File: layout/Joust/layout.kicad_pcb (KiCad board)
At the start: 4 copper layers, 30 x 30 mm, 56 parts, among them J1 B2B-PH-SM4-TB, J2 B2B-PH-SM4-TB, J3 TC2030-IDC-NL, J4 USB4105-GF-A, Q1 2N7002KT1G, Q2 2N7002KT1G, Q3 2N7002KT1G, U1 LSM6DSOXTR, U2 NORA-B206-00B, U3 BQ25185DLHR, U4 RT9013-33GB, U5 TPD4E05U06QDQARQ1, Y1 32.768kHz 7pF

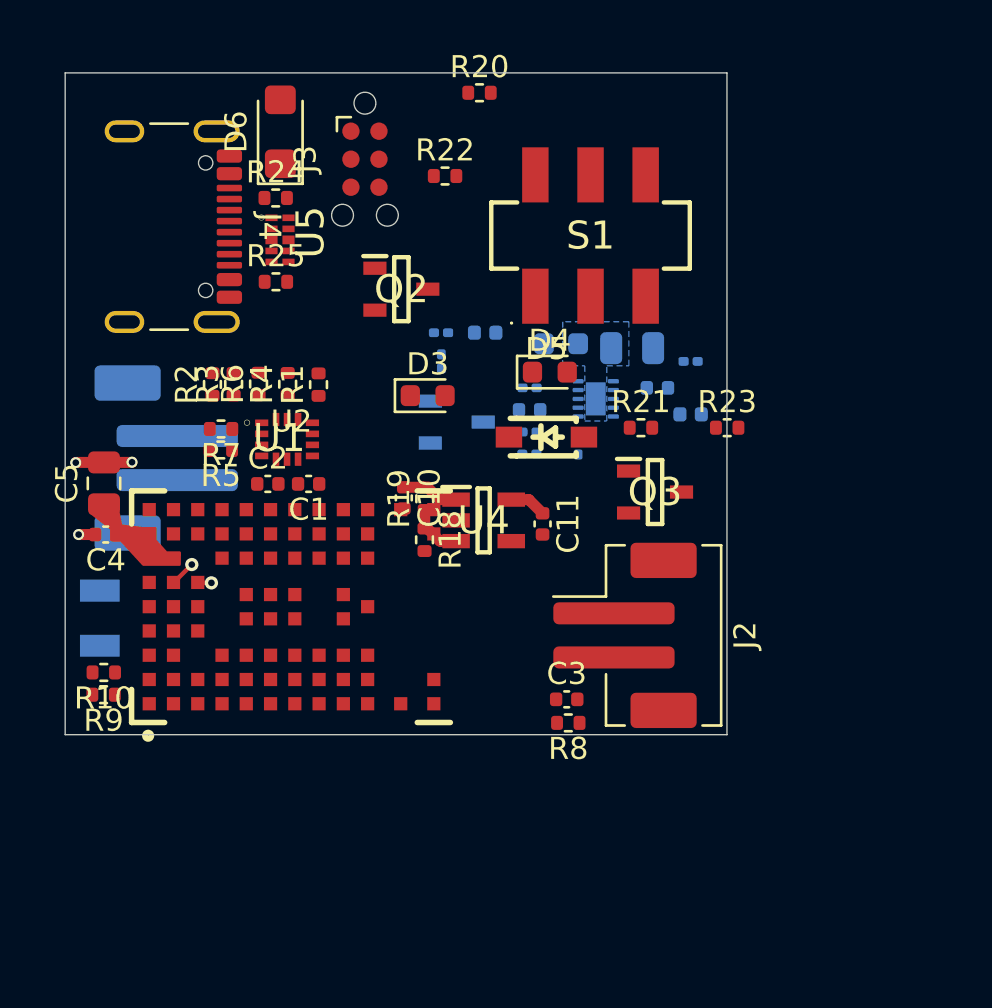
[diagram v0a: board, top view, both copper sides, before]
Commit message: remove bad traces
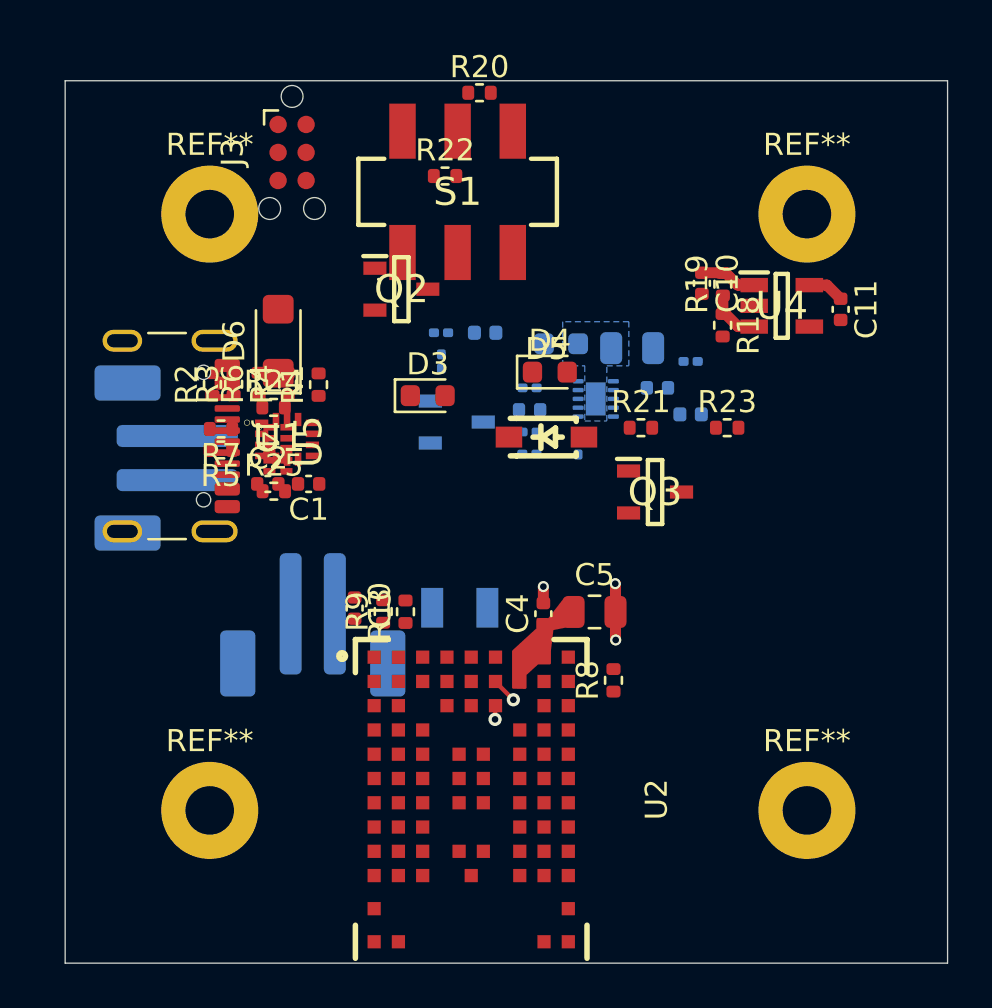
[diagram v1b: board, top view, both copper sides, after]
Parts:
- added REF**: MountingHole_2.2mm_M2_Pad, MountingHole:MountingHole_2.2mm_M2_Pad, F.Cu at (55.2, 65.9)
- added REF**: MountingHole_2.2mm_M2_Pad, MountingHole:MountingHole_2.2mm_M2_Pad, F.Cu at (82.2, 65.9)
- added REF**: MountingHole_2.2mm_M2_Pad, MountingHole:MountingHole_2.2mm_M2_Pad, F.Cu at (82.2, 93.0)
- added REF**: MountingHole_2.2mm_M2_Pad, MountingHole:MountingHole_2.2mm_M2_Pad, F.Cu at (55.2, 93.0)
- J2: moved to B.Cu
- moved C5 23.0 mm to (72.6, 84.0), turned to 0 degrees
- moved C4 20.2 mm to (70.3, 84.1), turned to 90 degrees
- moved C10 16.6 mm to (77.5, 69.1)
- moved C11 16.6 mm to (83.8, 70.3)
- moved R18 16.6 mm to (78.4, 71.0)
- moved R19 16.6 mm to (78.4, 69.1)
- moved U4 16.6 mm to (81.1, 70.1)
- moved Y1 16.3 mm to (66.5, 83.8), turned to 0 degrees
- moved J2 14.2 mm to (59.8, 84.6), turned to 0 degrees
- moved R10 13.9 mm to (64.0, 84.0), turned to 90 degrees
- moved R9 13.2 mm to (63.0, 84.0), turned to 90 degrees
- moved U2 11.9 mm to (67.0, 92.5), turned to -90 degrees
- moved C3 10.5 mm to (61.7, 83.8), turned to -90 degrees
- moved D6 9.49 mm to (58.3, 71.7)
- moved J4 9.49 mm to (52.3, 76.0)
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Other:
- board size 30 x 30 mm -> 40 x 40 mm
- copper layers 4 -> 2

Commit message: layout: 4-layer stackup, schematic placement, initial board sync
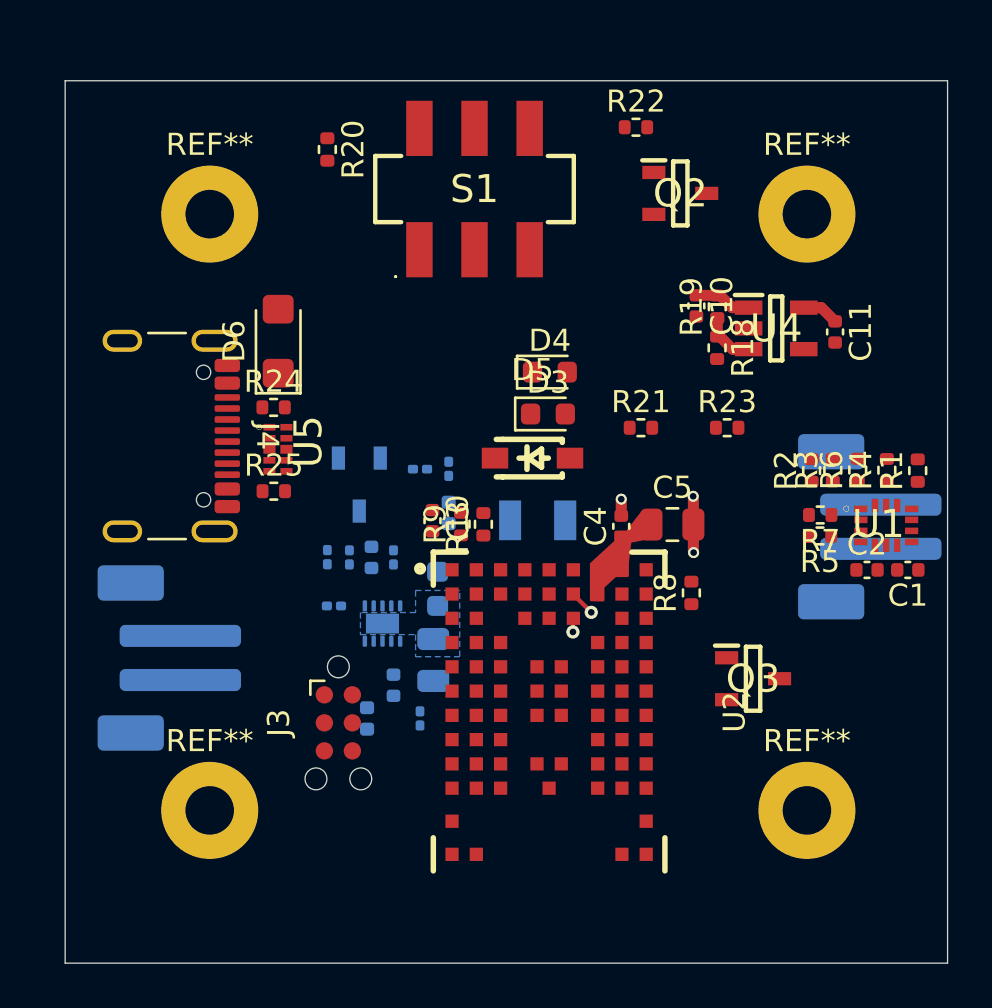
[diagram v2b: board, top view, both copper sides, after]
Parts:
- moved R1 27.4 mm to (87.3, 77.6)
- moved R6 27.4 mm to (84.5, 77.5)
- moved C1 27.4 mm to (86.8, 82.1)
- moved R2 27.4 mm to (82.5, 77.6)
- moved R4 27.4 mm to (85.9, 77.5)
- moved R7 27.4 mm to (82.8, 79.6)
- moved C2 27.4 mm to (85.0, 82.1)
- moved R3 27.4 mm to (83.4, 77.5)
- moved R5 27.4 mm to (82.8, 80.5)
- moved U1 27.4 mm to (85.8, 80.0)
- moved J3 25.9 mm to (61.0, 89.0)
- moved J2 25.6 mm to (85.1, 80.1), turned to -90 degrees
- moved R15 20.3 mm to (64.7, 88.8), turned to -90 degrees
- moved D2 20.1 mm to (62.3, 88.8), turned to -90 degrees
- moved C6 18.0 mm to (63.5, 87.3), turned to -90 degrees
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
